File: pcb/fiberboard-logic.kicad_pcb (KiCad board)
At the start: 2 copper layers, 118 x 84 mm, 117 parts, among them J1 VIN, J2 KB24, J3 FOOT, J4 NPN, J5 RLY1, J6 RLY2, J7 SOL, J8 RS485-2EDG3P, K1 G6KU-2F-Y, K2 G6KU-2F-Y, Q12 AO4407A, Q3 2N3904, Q4 2N3904, Q5 AO3400A, U1 ESP32-DevKitC-32E, U2 XL1509-5.0, U3 AMS1117-3.3, U5 PC817, U6 PC817, U7 MAX485E

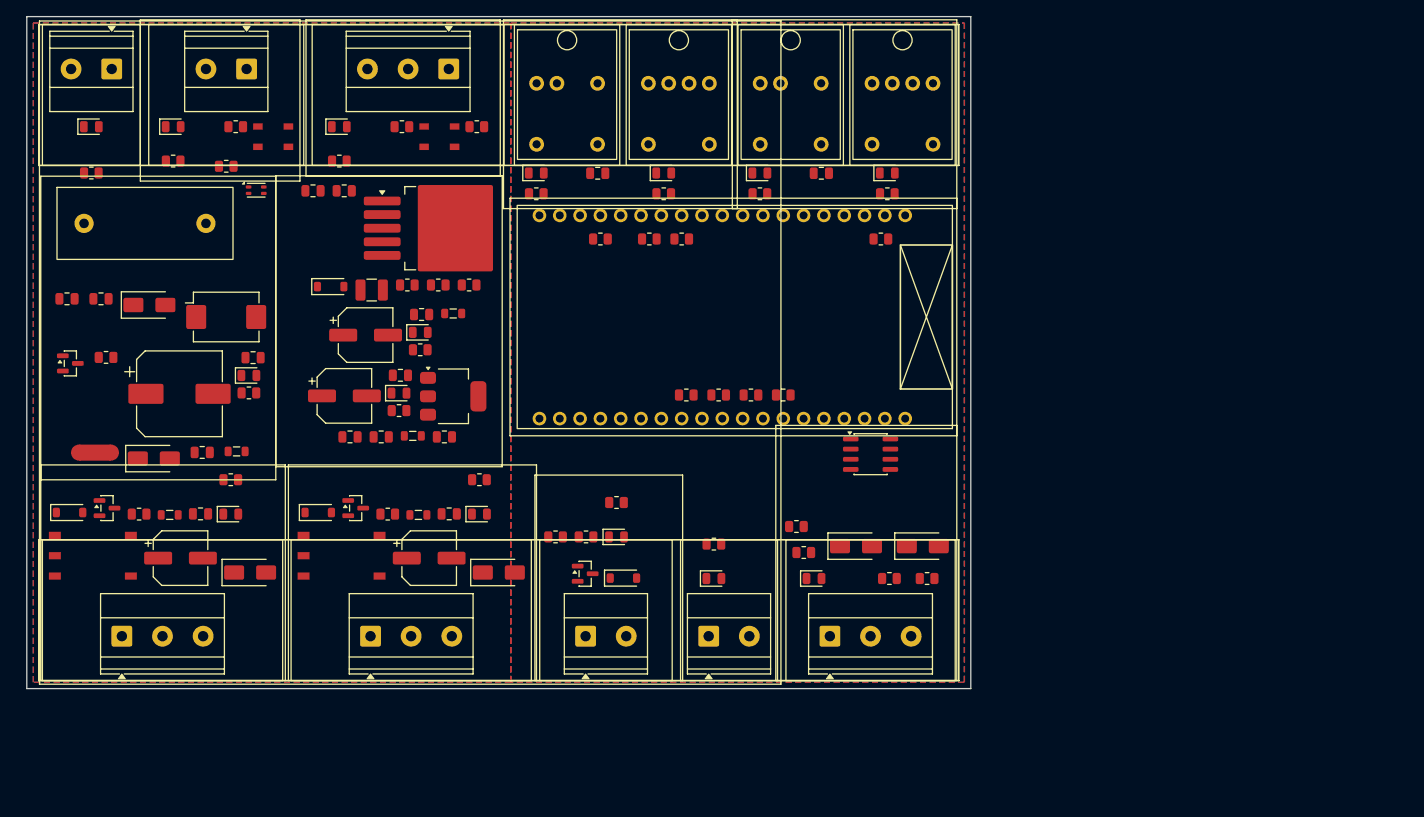
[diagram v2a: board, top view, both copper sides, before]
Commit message: update lại linh kiện để tối ưu thương mại. chuyển sang dùng cảm biến sợi quang rời, không tích hợp trên mạch nữa
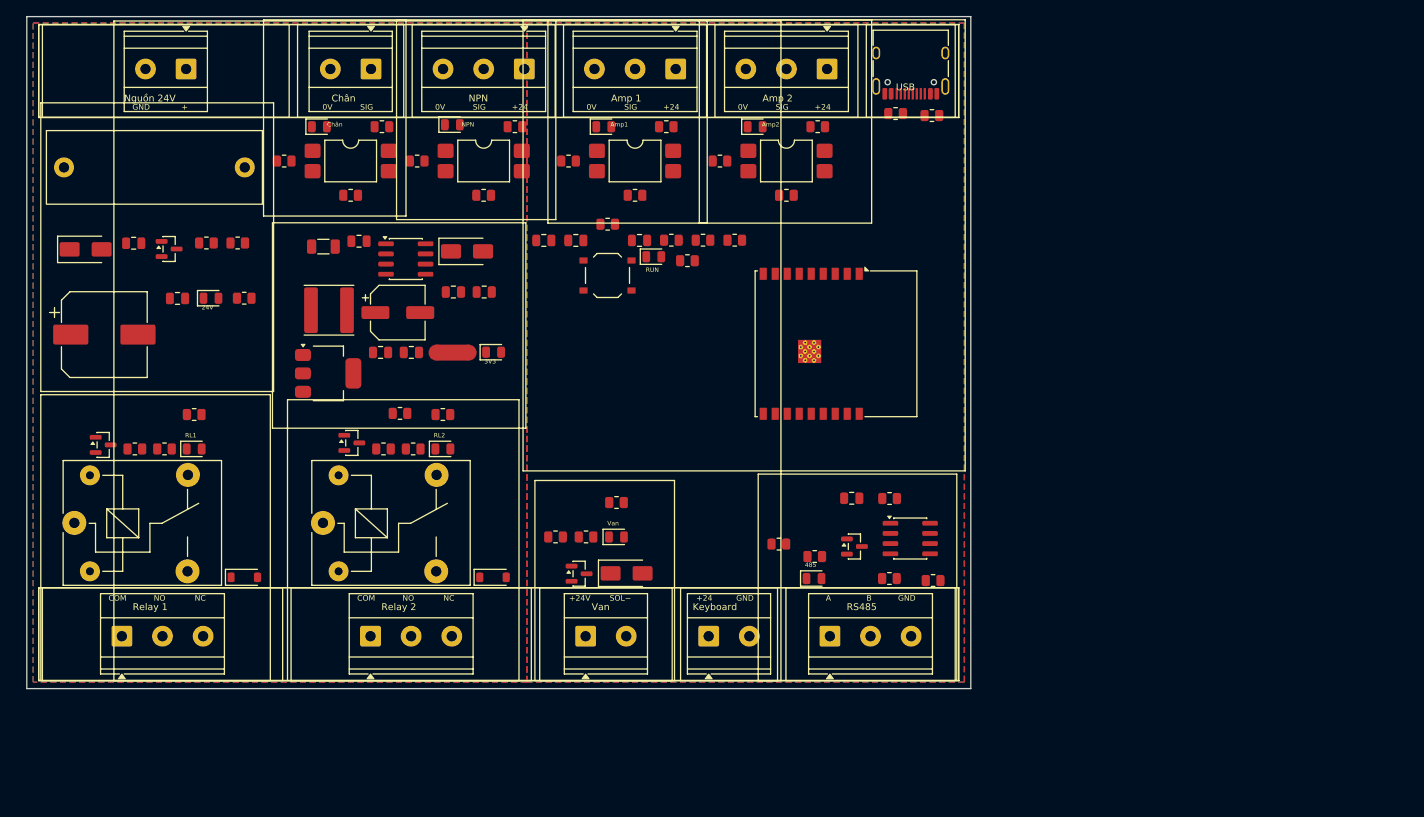
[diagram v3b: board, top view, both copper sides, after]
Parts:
- removed C12, C13, C21, C23, C25, C27: 100nF, Capacitor_SMD:C_0805_2012Metric
- removed C19: 10uF, Capacitor_SMD:C_0805_2012Metric
- removed C22, C24, C26: 220uF, Capacitor_SMD:CP_Elec_6.3x5.4
- removed D10, D11, D12, D26: SMAJ5.0A, Diode_SMD:D_SMA
- removed D13: VIN, LED_SMD:LED_0805_2012Metric
- removed D14: KB24, LED_SMD:LED_0805_2012Metric
- removed D21: TX1, LED_SMD:LED_0805_2012Metric
- removed D22: RX1, LED_SMD:LED_0805_2012Metric
- removed D23: TX2, LED_SMD:LED_0805_2012Metric
- removed D24: RX2, LED_SMD:LED_0805_2012Metric
- removed D25: 5V, LED_SMD:LED_0805_2012Metric
- removed F1R, F2R: AFBR-2624Z, Fiberboard:AFBR_2624Z_VL
- removed F1T, F2T: AFBR-1624Z, Fiberboard:AFBR_1624Z_VL
- removed FB1, FB2, FB3, FB4, FB5: BLM21PG121, Inductor_SMD:L_0805_2012Metric
- removed L2: ACM2012, Inductor_SMD:L_CommonModeChoke_Coilank_ACM2012
- removed R20, R21: 100k, Resistor_SMD:R_0805_2012Metric
- removed R22, R23, R38: 10k, Resistor_SMD:R_0805_2012Metric
- removed R30, R31, R32, R33, R34, R37, R40, R41, R42, R43, R44, R45: 1k, Resistor_SMD:R_0805_2012Metric
- removed R36: 3k, Resistor_SMD:R_0805_2012Metric
- removed RV1: MOV-26V, Varistor:Varistor_Panasonic_VF
- added C10: 1uF, Capacitor_SMD:C_0805_2012Metric, F.Cu at (76.6, 28.0)
- added C11: 100nF, Capacitor_SMD:C_0805_2012Metric, F.Cu at (103.1, 60.2)
- added C8: 10uF, Capacitor_SMD:C_0805_2012Metric, F.Cu at (64.6, 28.0)
- added C9: 100nF, Capacitor_SMD:C_0805_2012Metric, F.Cu at (68.6, 28.0)
- added D30: RUN, LED_SMD:LED_0805_2012Metric, F.Cu at (78.4, 30.0)
- added D31: AMP1, LED_SMD:LED_0805_2012Metric, F.Cu at (72.1, 13.8)
- added D32: AMP2, LED_SMD:LED_0805_2012Metric, F.Cu at (91.0, 13.8)
- added J10: AMP2, Fiberboard:Terminal_2EDG5.08-1x03_P5.08mm_Horizontal, F.Cu at (100.0, 6.55)
- added J11: USB-C, Connector_USB:USB_C_Receptacle_HRO_TYPE-C-31-M-12, F.Cu at (110.5, 5.60)
- added J9: AMP1, Fiberboard:Terminal_2EDG5.08-1x03_P5.08mm_Horizontal, F.Cu at (81.1, 6.55)
- added R47: 10k, Resistor_SMD:R_0805_2012Metric, F.Cu at (17.2, 54.0)
- added R48: 10k, Resistor_SMD:R_0805_2012Metric, F.Cu at (48.3, 54.0)
- added R49: 10k, Resistor_SMD:R_0805_2012Metric, F.Cu at (107.8, 60.2)
- added R50: 5.1k, Resistor_SMD:R_0805_2012Metric, F.Cu at (108.6, 12.1)
- added R51: 5.1k, Resistor_SMD:R_0805_2012Metric, F.Cu at (113.1, 12.4)
- added R52: 10k, Resistor_SMD:R_0805_2012Metric, F.Cu at (72.6, 25.9)
- added R53: 10k, Resistor_SMD:R_0805_2012Metric, F.Cu at (80.6, 27.9)
- added R54: 10k, Resistor_SMD:R_0805_2012Metric, F.Cu at (84.5, 27.9)
- added R55: 10k, Resistor_SMD:R_0805_2012Metric, F.Cu at (88.5, 27.9)
- added R56: 1k, Resistor_SMD:R_0805_2012Metric, F.Cu at (82.6, 30.5)
- added R57: 10k, Resistor_SMD:R_0805_2012Metric, F.Cu at (79.9, 13.8)
- added R58: 10k, Resistor_SMD:R_0805_2012Metric, F.Cu at (76.0, 22.3)
- added R59: 1k, Resistor_SMD:R_0805_2012Metric, F.Cu at (67.7, 18.1)
- added R60: 10k, Resistor_SMD:R_0805_2012Metric, F.Cu at (98.9, 13.8)
- added R61: 10k, Resistor_SMD:R_0805_2012Metric, F.Cu at (95.0, 22.3)
- added R62: 1k, Resistor_SMD:R_0805_2012Metric, F.Cu at (86.6, 18.1)
- added R63: 10k, Resistor_SMD:R_0805_2012Metric, F.Cu at (26.4, 28.3)
- added SW1: BOOT, Button_Switch_SMD:SW_Push_1P1T_XKB_TS-1187A, F.Cu at (72.6, 32.4)
- added U10: LTV-817S, Package_DIP:SMDIP-4_W9.53mm, F.Cu at (95.0, 18.1)
- added U9: LTV-817S, Package_DIP:SMDIP-4_W9.53mm, F.Cu at (76.0, 18.1)
- C14, C15, C17: value 100nF -> 100nF 50V
- C16: value 10uF -> 10uF 50V; footprint Capacitor_SMD:C_0805_2012Metric -> Capacitor_SMD:C_1206_3216Metric
- C2: value 220uF -> 220uF 10V
- C4: value 1000uF -> 470uF 35V; footprint Capacitor_SMD:CP_Elec_10x12.5 -> Capacitor_SMD:CP_Elec_10x10.5
- D3, D4: value SS34 -> 1N4148W
- D5, D8: footprint Diode_SMD:D_SOD-123 -> Diode_SMD:D_SMA
- D7: value SMAJ28A -> SMAJ26A
- D9: value SMAJ5.0A -> PSM712; footprint Diode_SMD:D_SMA -> Package_TO_SOT_SMD:SOT-23
- F1: value 5x20 F4A -> 5x20 su 4A; footprint Fiberboard:Fuseholder_5x20mm_Horizontal -> Fiberboard:Fuseholder_5x20mm_Covered
- J8: value RS485-2EDG3P -> RS485
- K1, K2: value G6KU-2F-Y -> HF3FF-024-1ZS; footprint Fiberboard:G6KU-2F_SMD -> Relay_THT:Relay_SPDT_SANYOU_SRD_Series_Form_C
- L1: value 47uH -> 47uH 6045; footprint Inductor_SMD:L_1210_3225Metric -> Inductor_SMD:L_Sunlord_SWPA6045S
- Q12: value AO4407A -> AO3401A
- Q3, Q4: value 2N3904 -> MMBT3904
- R13: value 100 -> 10R
- R15: value 100 -> 120R
- R17: value 100k -> 27k
- R26, R27, R7, R8: value 1k -> 10k
- U1: value ESP32-DevKitC-32E -> ESP32-C3-WROOM-02; footprint Fiberboard:ESP32_DevKitC_Socket -> RF_Module:ESP32-C3-WROOM-02
- U2: footprint Package_TO_SOT_SMD:TO-263-5_TabPin3 -> Package_SO:SOIC-8_3.9x4.9mm_P1.27mm
- U5, U6: value PC817 -> LTV-817S; footprint Fiberboard:PC817_SO4 -> Package_DIP:SMDIP-4_W9.53mm
- U7: value MAX485E -> SP3485EN
- moved NT1 46.4 mm to (53.2, 42.0)
- moved D3 23.3 mm to (27.2, 70.1)
- moved D4 23.3 mm to (58.3, 70.1)
- moved R17 19.0 mm to (22.4, 28.3)
- moved Q12 18.9 mm to (17.8, 29.1)
- moved R7 18.3 mm to (44.4, 13.8)
- moved D15 18.3 mm to (36.6, 13.8)
- moved D8 17.6 mm to (55.0, 29.4)
- moved R9 16.0 mm to (40.5, 22.3)
- moved U3 15.9 mm to (37.7, 44.6)
- moved J3 15.6 mm to (43.0, 6.55)
- moved C7 14.8 mm to (57.2, 34.4)
- moved D16 14.1 mm to (53.2, 13.5)
- moved R8 14.1 mm to (61.0, 13.8)
- moved R24 13.9 mm to (32.2, 18.1)
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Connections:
- net +5V_SW renamed BUCK_SW
- C18 pad 1: +3V3_REG -> +3V3
- C2 pad 1: +5V_RAW -> +5V
- C2 pad 2: GND -> GND_PWR
- C3 pad 1: +3V3_REG -> +3V3
- C5 pad 1: +5V_RAW -> +5V
- C5 pad 2: GND -> GND_PWR
- D3 pad 1: +5V_RLY1 -> +24V
- D4 pad 1: +5V_RLY2 -> +24V
- D9 pad 2: GND -> RS485_B_BUS
- F1 pad 2: VIN_CM_IN -> VIN_FUSE
- J1 pad 2: VIN_CM_RET -> GND_PWR
- J3 pad 1: FOOT_A -> FOOT_SIG
- J3 pad 2: FOOT_K -> GND_PWR
- J4 pad 1: NPN_V+ -> +24V
- K1 pad 1: +5V_RLY1 -> RLY1_COM
- K1 pad 4: RLY1_COM -> RLY1_NC
- K1 pad 5: RLY1_NC -> +24V
- K2 pad 1: +5V_RLY2 -> RLY2_COM
- K2 pad 4: RLY2_COM -> RLY2_NC
- K2 pad 5: RLY2_NC -> +24V
- L1 pad 2: +5V_RAW -> +5V
- NT1 pad 2: GND_SPLICE -> GND
- Q12 pad 2: VIN_FUSE -> +24V
- Q12 pad 3: +24V -> VIN_FUSE
- Q3 pad 1: GND_PWR -> RLY1_B
- Q3 pad 2: RLY1_B -> GND_PWR
- Q4 pad 1: GND_PWR -> RLY2_B
- Q4 pad 2: RLY2_B -> GND_PWR
- R26 pad 1: +5V_RLY1 -> +24V
- R27 pad 1: +5V_RLY2 -> +24V
- R7 pad 1: FOOT_A -> +24V
- R8 pad 1: NPN_SIG -> +24V
- U1 pad 10: IN_NPN -> OUT_MOS
- U1 pad 11: OUT_RLY1 -> RS485_RX
- U1 pad 12: OUT_RLY2 -> RS485_TX
- U1 pad 13: (no net) -> USB_DN
- U1 pad 14: GND -> USB_DP
- U1 pad 15: OUT_MOS -> RS485_DE
- U1 pad 16: (no net) -> ESP_IO2
- U1 pad 17: (no net) -> OUT_RLY2
- U1 pad 18: (no net) -> OUT_RLY1
- U1 pad 19: +5V -> GND
- U1 pad 2: +3V3 -> ESP_EN
- U1 pad 3: (no net) -> IN_FOOT
- U1 pad 4: (no net) -> IN_NPN
- U1 pad 5: (no net) -> IN_AMP1
- U1 pad 6: (no net) -> IN_AMP2
- U1 pad 7: FIBER1_PWM -> LED_RUN
- U1 pad 8: FIBER2_PWM -> ESP_BOOT
- U1 pad 9: IN_FOOT -> GND
- U2 pad 3: BUCK_FB -> +5V
- U2 pad 4: BUCK_EN -> GND_PWR
- U3 pad 2: +3V3_REG -> +3V3
- U5 pad 2: FOOT_K -> FOOT_SIG
- U6 pad 2: GND_PWR -> NPN_SIG
- U7 pad 1: RS485_RO -> RS485_RX
- U7 pad 4: RS485_DI -> RS485_TX
- U7 pad 8: +5V -> +3V3
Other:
- board text added: "0V"
- board text added: "485"
- board text added: "Amp 1"
- board text added: "Amp 2"
- board text added: "Amp1"
- board text added: "Amp2"
- board text added: "Bắt buộc: MCU + USB"
- board text added: "Bắt buộc: buck 5 V + LDO 3,3 V"
- board text added: "C 100nF 50V"
- board text added: "C 10uF 50V"
- board text added: "C 1uF"
- board text added: "C 220uF 10V"
- board text added: "C 470uF 35V"
- board text added: "Nguồn 24V"
- board text added: "R 120R"
- board text added: "R 27k"
- board text added: "R 5.1k"
- board text added: "RL1"
- board text added: "RL2"
- board text added: "RS485"
- board text added: "RUN"
- board text added: "Tùy chọn: J10 amp 2"
- board text added: "Tùy chọn: J9 amp 1"
- board text added: "USB"
- board text removed: "5V"
- board text removed: "Bắt buộc: MCU"
- board text removed: "Bắt buộc: buck 5 V / LDO 3,3 V"
- board text removed: "C 1000uF"
- board text removed: "C 220uF"
- board text removed: "K"
- board text removed: "Nguồn"
- board text removed: "PWM"
- board text removed: "Q1 phát"
- board text removed: "Q1 thu"
- board text removed: "Q2 phát"
- board text removed: "Q2 thu"
- board text removed: "R 100"
- board text removed: "R 100k"
- board text removed: "R 3k"
- board text removed: "RS485 cắm"
- board text removed: "TTL"
- board text removed: "Tùy chọn: quang kênh 1"
- board text removed: "Tùy chọn: quang kênh 2"
- board text removed: "V+"
